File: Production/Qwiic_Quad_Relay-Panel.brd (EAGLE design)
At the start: 82.5 x 47 mm, 119 parts, among them J2 Qwiic Right Angle, J3 Qwiic Right Angle, J4 AVR_SPI_PROG_3X2TESTPOINTS, J9 POWER_JACK, K1 RELAY-SPDT-JZC-11F, K2 RELAY-SPDT-JZC-11F, K3 RELAY-SPDT-JZC-11F, K4 RELAY-SPDT-JZC-11F, Q1 600mA/40V, Q2 600mA/40V, Q3 600mA/40V, Q4 600mA/40V, U1 V_REG_317SMD, U2 DUAL-OPTOISOLATOR_SOIC8, U3 DUAL-OPTOISOLATOR_SOIC8, U5 ATTINY84-ARDUINO

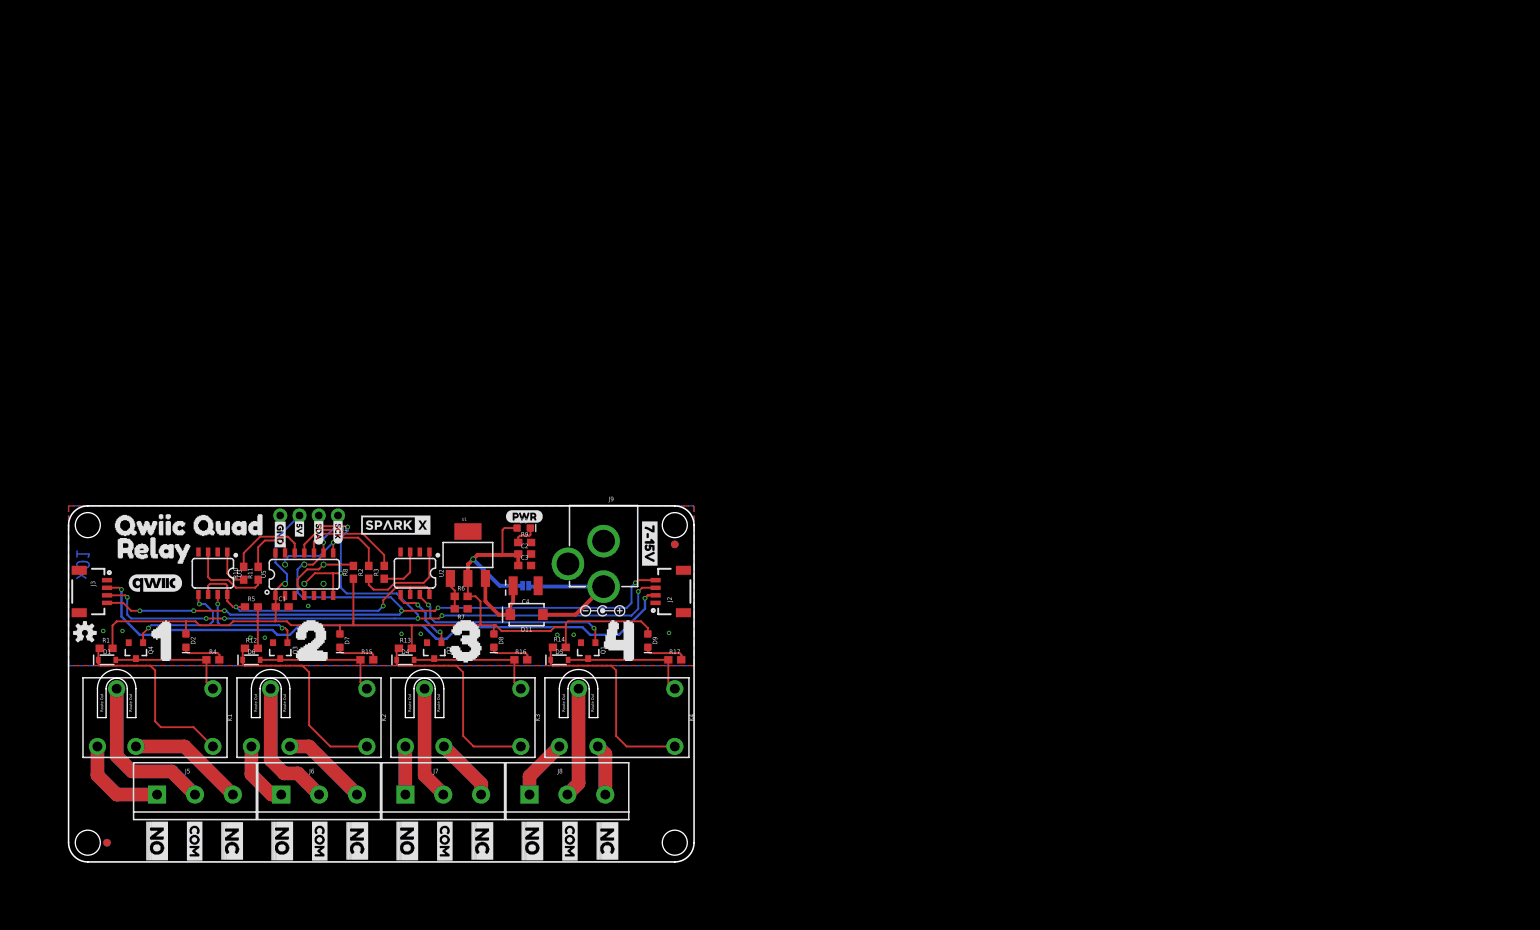
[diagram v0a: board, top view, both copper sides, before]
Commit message: Changed internal route out to milling, also production files.
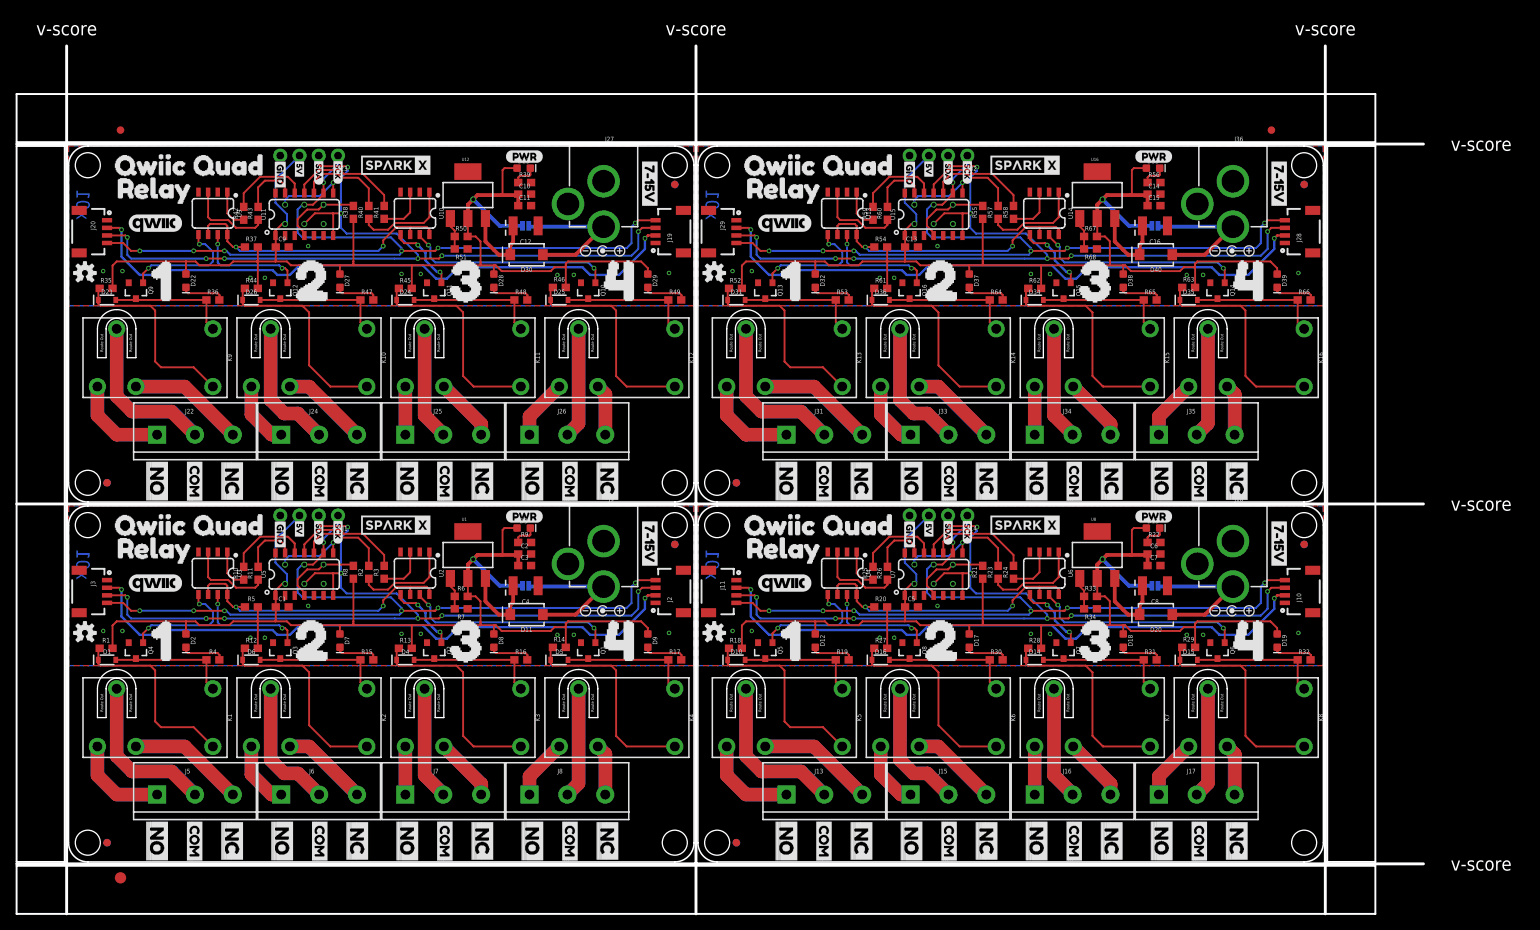
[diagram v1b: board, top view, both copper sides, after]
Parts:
- removed FRAME1: FRAME-LETTER, SparkFun-Aesthetics:CREATIVE_COMMONS
- added C10, C14, C6: 10uF, SparkFun-Capacitors:0603
- added C11, C13, C15, C5, C7, C9: 0.1uF, SparkFun-Capacitors:0603
- added C12, C16, C8: 10uF, SparkFun-Capacitors:EIA3528
- added D10, D14, D15, D16, D21, D24, D25, D26, D31, D34, D35, D36: 1A/23V/620mV, SparkFun-DiscreteSemi:SOD-323
- added D12, D22, D32: WHITE, SparkFun-LED:LED-0603
- added D13, D23, D33: RED, SparkFun-LED:LED-0603
- added D17, D27, D37: BLUE, SparkFun-LED:LED-0603
- added D18, D28, D38: Yellow, SparkFun-LED:LED-0603
- added D19, D29, D39: GREEN, SparkFun-LED:LED-0603
- added D20, D30, D40: 1A/40V/500mV, SparkFun-DiscreteSemi:SMA-DIODE
- added E$1, E$2: (no value), SparkFun-Aesthetics:FIDUCIAL-1X2
- added E$3: (no value), SparkFun-Retired:FIDUCIAL-1.5X3
- added J10, J11, J19, J20, J28, J29: Qwiic Right Angle, SparkFun-Connectors:1X04_1MM_RA
- added J12, J21, J30: AVR_SPI_PROG_3X2TESTPOINTS, SparkFun-Connectors:2X3_TEST_POINTS
- added J13, J15, J16, J17, J22, J24, J25, J26, J31, J33, J34, J35: (no value), SparkFun-Connectors:SCREWTERMINAL-5MM-3
- added J14, J23, J32: (no value), SparkFun-Connectors:1X04_NO_SILK
- added J18, J27, J36: POWER_JACK, SparkFun-Connectors:POWER_JACK_PTH
- added JP10, JP11, JP14, JP15, JP19, JP20, JP23, JP24, JP28, JP29, JP32, JP33: STAND-OFF, SparkFun:STAND-OFF
- added JP12, JP13, JP16, JP17, JP21, JP22, JP25, JP26, JP30, JP31, JP34, JP35: FIDUCIAL1X2, SparkFun-Aesthetics:FIDUCIAL-1X2
- added JP18, JP27, JP36: JUMPER-SMT_2_NO_SILK, SparkFun-Jumpers:SMT-JUMPER_2_NO_SILK
- added K10, K11, K12, K13, K14, K15, K16, K5, K6, K7, K8, K9: RELAY-SPDT-JZC-11F, SparkFun-Electromechanical:RELAY-JZC
- added LOGO2, LOGO3, LOGO4: OSHW-LOGOS, SparkFun-Aesthetics:OSHW-LOGO-S
- added Q10, Q11, Q12, Q13, Q14, Q15, Q16, Q5, Q6, Q7, Q8, Q9: 600mA/40V, SparkFun-DiscreteSemi:SOT23-3
- added R18, R27, R28, R29, R35, R44, R45, R46, R52, R61, R62, R63: 10, SparkFun-Resistors:0603
- added R19, R20, R23, R24, R25, R26, R30, R31, R32, R36, R37, R40, R41, R42, R43, R47, R48, R49, R53, R54, R57, R58, R59, R60, R64, R65, R66: 220, SparkFun-Resistors:0603
- added R21, R38, R55: 10K, SparkFun-Resistors:0603
- added R22, R39, R56: 1k, SparkFun-Resistors:0603
- added R33, R50, R67: 240, SparkFun-Resistors:0603
- added R34, R51, R68: 715, SparkFun-Resistors:0603
- added U$100, U$103, U$156, U$159, U$212, U$215: (no value), 5V:5V0
- added U$101, U$104, U$157, U$160, U$213, U$216: (no value), SDA:SDA0
- added U$102, U$155, U$158, U$211, U$214, U$99: (no value), Labels:GND-03
- added U$105, U$154, U$161, U$210, U$217, U$98: (no value), Labels:SCK-[)-03
- added U$106, U$108, U$162, U$164, U$218, U$220: (no value), Polarity_marking_center_positive#jpg:POLARITY_MARKING_CENTER_POSITIVE#JPG
- added U$107, U$153, U$163, U$209, U$219, U$97: (no value), 7-15V:7#15V0
- added U$109, U$110, U$165, U$166, U$221, U$222: (no value), qwiic_copyrighted_logo_medium:QWIIC#JPG
- added U$111, U$167, U$223: (no value), 5V Wall Adapter:5V_WALL_ADAPTER0
- added U$112, U$168, U$224: (no value), jumper:JUMPER0
- added U$113, U$169, U$56: (no value), Labels:PWR-()-04
- added U$114, U$147, U$170, U$203, U$58, U$91: (no value), 2:20
- added U$115, U$146, U$171, U$202, U$59, U$90: (no value), 1:10
- added U$116, U$148, U$172, U$204, U$60, U$92: (no value), 3:30
- added U$117, U$149, U$173, U$205, U$61, U$93: (no value), 4:40
- added U$118, U$150, U$174, U$206, U$62, U$94: (no value), Quad:QWIIC_QUAD_0
- added U$119, U$151, U$175, U$207, U$63, U$95: (no value), relay:RELAY0
- added U$120, U$176, U$64: SPARKX-LOGO4, SparkX:SPARKX-MEDIUM
- added U$121, U$177, U$65: (no value), SparkX:SPARKX-MEDIUM
- added U$122, U$125, U$128, U$131, U$134, U$137, U$140, U$143, U$178, U$181, U$184, U$187, U$190, U$193, U$196, U$199, U$66, U$69, U$72, U$75, U$78, U$81, U$84, U$87: (no value), NO:NO0
- added U$123, U$126, U$129, U$132, U$135, U$138, U$141, U$144, U$179, U$182, U$185, U$188, U$191, U$194, U$197, U$200, U$67, U$70, U$73, U$76, U$79, U$82, U$85, U$88: (no value), COM:COM0
- added U$124, U$127, U$130, U$133, U$136, U$139, U$142, U$145, U$180, U$183, U$186, U$189, U$192, U$195, U$198, U$201, U$68, U$71, U$74, U$77, U$80, U$83, U$86, U$89: (no value), NC:NC0
- added U$152, U$208, U$96: (no value), SparkFun-Aesthetics:OSHW-LOGO-S
- added U10, U13, U14, U4, U6, U9: DUAL-OPTOISOLATOR_SOIC8, SparkFun-DiscreteSemi:SO08
- added U11, U15, U7: ATTINY84-ARDUINO, SparkFun-IC-Microcontroller:SO14
- added U12, U16, U8: V_REG_317SMD, SparkFun-IC-Power:SOT223
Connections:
- new net !RESET1: J12.5, R21.2, U7.4
- new net !RESET2: J21.5, R38.2, U11.4
- new net !RESET3: J30.5, R55.2, U15.4
- new net 3.3V1: J10.2, J11.2
- new net 3.3V2: J19.2, J20.2
- new net 3.3V3: J28.2, J29.2
- new net 5V1: C5.1, C6.1, C7.1, D12.A, D13.A, D17.A, D18.A, D19.A, J12.2, J14.3, JP18.2, R18.2, R20.2, R21.1, R27.2, R28.2, R29.2, R33.2, U7.1, U8.2
- new net 5V2: C10.1, C11.1, C9.1, D22.A, D23.A, D27.A, D28.A, D29.A, J21.2, J23.3, JP27.2, R35.2, R37.2, R38.1, R44.2, R45.2, R46.2, R50.2, U11.1, U12.2
- new net 5V3: C13.1, C14.1, C15.1, D32.A, D33.A, D37.A, D38.A, D39.A, J30.2, J32.3, JP36.2, R52.2, R54.2, R55.1, R61.2, R62.2, R63.2, R67.2, U15.1, U16.2
- new net COM10: J24.2, K10.4
- new net COM11: J25.2, K11.4
- new net COM12: J26.2, K12.4
- new net COM13: J31.2, K13.4
- new net COM14: J33.2, K14.4
- new net COM15: J34.2, K15.4
- new net COM16: J35.2, K16.4
- new net COM5: J13.2, K5.4
- new net COM6: J15.2, K6.4
- new net COM7: J16.2, K7.4
- new net COM8: J17.2, K8.4
- new net COM9: J22.2, K9.4
- new net GND1: C5.2, C6.2, C7.2, C8.C, J10.1, J11.1, J12.6, J14.4, J18.GND, J18.GNDBREAK, Q5.2, Q6.2, Q7.2, Q8.2, R22.2, R34.1, U4.2, U4.4, U6.2, U6.4, U7.14
- new net GND2: C10.2, C11.2, C12.C, C9.2, J19.1, J20.1, J21.6, J23.4, J27.GND, J27.GNDBREAK, Q10.2, Q11.2, Q12.2, Q9.2, R39.2, R51.1, U10.2, U10.4, U11.14, U9.2, U9.4
- new net GND3: C13.2, C14.2, C15.2, C16.C, J28.1, J29.1, J30.6, J32.4, J36.GND, J36.GNDBREAK, Q13.2, Q14.2, Q15.2, Q16.2, R56.2, R68.1, U13.2, U13.4, U14.2, U14.4, U15.14
- new net MISO1: J12.1, U7.8
- new net MISO2: J21.1, U11.8
- new net MISO3: J30.1, U15.8
- new net N$10: D10.A, K5.1, Q5.3, R19.1
- new net N$18: D10.C, K5.5, R18.1
- new net N$23: D12.C, R19.2
- new net N$24: D13.C, R22.1
- new net N$25: R26.1, U4.3
- new net N$26: R25.1, U4.1
- new net N$27: R20.1, U4.6, U4.8, U6.6, U6.8
- new net N$28: R23.1, U6.1
- new net N$29: R24.1, U6.3
- new net N$30: D16.C, K6.5, R27.1
- new net N$31: D16.A, K6.1, Q8.3, R30.1
- new net N$32: D14.C, K7.5, R28.1
- new net N$33: D14.A, K7.1, Q7.3, R31.1
- new net N$34: D15.C, K8.5, R29.1
- new net N$35: D15.A, K8.1, Q6.3, R32.1
- new net N$36: D19.C, R32.2
- new net N$37: D18.C, R31.2
- new net N$38: D17.C, R30.2
- new net N$39: R33.1, R34.2, U8.1
- new net N$40: C8.A, D20.C, U8.3
- new net N$41: D21.A, K9.1, Q9.3, R36.1
- new net N$42: D21.C, K9.5, R35.1
- new net N$43: D22.C, R36.2
- new net N$44: D23.C, R39.1
- new net N$45: R43.1, U9.3
- new net N$46: R42.1, U9.1
- new net N$47: R37.1, U10.6, U10.8, U9.6, U9.8
- new net N$48: R40.1, U10.1
- new net N$49: R41.1, U10.3
- new net N$50: D26.C, K10.5, R44.1
- new net N$51: D26.A, K10.1, Q12.3, R47.1
- new net N$52: D24.C, K11.5, R45.1
- new net N$53: D24.A, K11.1, Q11.3, R48.1
- new net N$54: D25.C, K12.5, R46.1
- new net N$55: D25.A, K12.1, Q10.3, R49.1
- new net N$56: D29.C, R49.2
- new net N$57: D28.C, R48.2
- new net N$58: D27.C, R47.2
- new net N$59: R50.1, R51.2, U12.1
- new net N$60: C12.A, D30.C, U12.3
- new net N$61: D31.A, K13.1, Q13.3, R53.1
- new net N$62: D31.C, K13.5, R52.1
- new net N$63: D32.C, R53.2
- new net N$64: D33.C, R56.1
- new net N$65: R60.1, U13.3
- new net N$66: R59.1, U13.1
- new net N$67: R54.1, U13.6, U13.8, U14.6, U14.8
- new net N$68: R57.1, U14.1
- new net N$69: R58.1, U14.3
- new net N$70: D36.C, K14.5, R61.1
- new net N$71: D36.A, K14.1, Q16.3, R64.1
- new net N$72: D34.C, K15.5, R62.1
- new net N$73: D34.A, K15.1, Q15.3, R65.1
- new net N$74: D35.C, K16.5, R63.1
- new net N$75: D35.A, K16.1, Q14.3, R66.1
- new net N$76: D39.C, R66.2
- new net N$77: D38.C, R65.2
- new net N$78: D37.C, R64.2
- new net N$79: R67.1, R68.2, U16.1
- new net N$80: C16.A, D40.C, U16.3
- new net NC10: J24.3, K10.2
- new net NC11: J25.3, K11.2
- new net NC12: J26.3, K12.2
- new net NC13: J31.3, K13.2
- new net NC14: J33.3, K14.2
- new net NC15: J34.3, K15.2
- new net NC16: J35.3, K16.2
- new net NC5: J13.3, K5.2
- new net NC6: J15.3, K6.2
- new net NC7: J16.3, K7.2
- new net NC8: J17.3, K8.2
- new net NC9: J22.3, K9.2
- new net NO10: J24.1, K10.3
- new net NO11: J25.1, K11.3
- new net NO12: J26.1, K12.3
- new net NO13: J31.1, K13.3
- new net NO14: J33.1, K14.3
- new net NO15: J34.1, K15.3
- new net NO16: J35.1, K16.3
- new net NO5: J13.1, K5.3
- new net NO6: J15.1, K6.3
- new net NO7: J16.1, K7.3
- new net NO8: J17.1, K8.3
- new net NO9: J22.1, K9.3
- new net OPTO_10: Q12.1, U9.7
- new net OPTO_11: Q11.1, U10.5
- new net OPTO_12: Q10.1, U10.7
- new net OPTO_13: Q13.1, U13.5
- new net OPTO_14: Q16.1, U13.7
- new net OPTO_15: Q15.1, U14.5
- new net OPTO_16: Q14.1, U14.7
- new net OPTO_5: Q5.1, U4.5
- new net OPTO_6: Q8.1, U4.7
- new net OPTO_7: Q7.1, U6.5
- new net OPTO_8: Q6.1, U6.7
- new net OPTO_9: Q9.1, U9.5
- new net RELAY_CTRL10: R41.2, U11.11
- new net RELAY_CTRL11: R42.2, U11.12
- new net RELAY_CTRL12: R43.2, U11.13
- new net RELAY_CTRL13: R57.2, U15.10
- new net RELAY_CTRL14: R58.2, U15.11
- new net RELAY_CTRL15: R59.2, U15.12
- new net RELAY_CTRL16: R60.2, U15.13
- new net RELAY_CTRL5: R23.2, U7.10
- new net RELAY_CTRL6: R24.2, U7.11
- new net RELAY_CTRL7: R25.2, U7.12
- new net RELAY_CTRL8: R26.2, U7.13
- new net RELAY_CTRL9: R40.2, U11.10
- new net SCL/SCK1: J10.4, J11.4, J12.3, J14.1, U7.9
- new net SCL/SCK2: J19.4, J20.4, J21.3, J23.1, U11.9
- new net SCL/SCK3: J28.4, J29.4, J30.3, J32.1, U15.9
- new net SDA/MOSI1: J10.3, J11.3, J12.4, J14.2, U7.7
- new net SDA/MOSI2: J19.3, J20.3, J21.4, J23.2, U11.7
- new net SDA/MOSI3: J28.3, J29.3, J30.4, J32.2, U15.7
- new net VIN1: D20.A, J18.PWR, JP18.1
- new net VIN2: D30.A, J27.PWR, JP27.1
- new net VIN3: D40.A, J36.PWR, JP36.1
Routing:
- net 5V3: track 0.00 -> 146.4 mm, vias 0 -> 1
- net 5V2: track 0.00 -> 146.4 mm, vias 0 -> 1
- net 5V1: track 0.00 -> 146.4 mm, vias 0 -> 1
- net SDA/MOSI2: track 0.00 -> 112.0 mm, vias 0 -> 8
- net SDA/MOSI3: track 0.00 -> 112.0 mm, vias 0 -> 8
- net SDA/MOSI1: track 0.00 -> 112.0 mm, vias 0 -> 8
- net SCL/SCK2: track 0.00 -> 104.6 mm, vias 0 -> 7
- net SCL/SCK3: track 0.00 -> 104.6 mm, vias 0 -> 7
- net SCL/SCK1: track 0.00 -> 104.6 mm, vias 0 -> 7
- net 3.3V3: track 0.00 -> 82.9 mm, vias 0 -> 2
- net 3.3V2: track 0.00 -> 82.9 mm, vias 0 -> 2
- net 3.3V1: track 0.00 -> 82.9 mm, vias 0 -> 2
- net COM13: track 0.00 -> 42.7 mm
- net COM9: track 0.00 -> 42.7 mm
- net COM5: track 0.00 -> 42.7 mm
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- added copper zone on layer 1, net GND1
- added copper zone on layer 16, net GND1
- added copper zone on layer 1, net GND2
- added copper zone on layer 16, net GND2
- added copper zone on layer 1, net GND3
- added copper zone on layer 16, net GND3
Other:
- board size 82.5 x 47 mm -> 185.7 x 114.6 mm
- board text added: "v-score"
- board text removed: "Elias Santistevan"
